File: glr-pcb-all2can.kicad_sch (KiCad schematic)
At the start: 19 parts, among them J1 Conn_02x04_Top_Bottom, J2 DA15_Pins_MountingHoles, U1 STM32F303K8T6, U2 173020536, U3 173010535

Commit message: add in- and outputs
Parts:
- added J3: Conn_01x04, Connector_PinSocket_2.54mm:PinSocket_1x04_P2.54mm_Vertical, symbol Connector_Generic:Conn_01x04
- renumbered C3 to C1, C4 to C2, C2 to C3, C6 to C4, C7 to C6, D2 to D1, D3 to D2, D4 to D3, D5 to D4, J2 to J1, J1 to J2, R5 to R1, R6 to R2
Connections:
- net +3.3V is gone; now on net +3V3: C1.2, C3.2, J2.5 (Pin_5), R1.1, R3.2, R4.2, U1.1 (VDD), U1.17 (VDD), U1.5 (VDDA)
- net Input filter/5_IN_INT: now reaches U1.10 (PA4)
- net Input filter/6_IN_INT: now reaches U1.11 (PA5)
- net Input filter/7_IN_INT: now reaches U1.12 (PA6)
- net Output/1_OUT_INT: now reaches U1.14 (PB0)
- net Output/2_OUT_INT: now reaches U1.15 (PB1)
- net at U1.25 (PA15): now also J3.4 (Pin_4)
- net at U1.26 (PB3): now also J3.1 (Pin_1)
- net at U1.27 (PB4): now also J3.2 (Pin_2)
- net at U1.28 (PB5): now also J3.3 (Pin_3)
- net Output/3_OUT_INT: now reaches U1.29 (PB6)
- net Output/4_OUT_INT: now reaches U1.30 (PB7)
- net Input filter/1_IN_INT: now reaches U1.6 (PA0)
- net Input filter/2_IN_INT: now reaches U1.7 (PA1)
- net Input filter/3_IN_INT: now reaches U1.8 (PA2)
- net Input filter/4_IN_INT: now reaches U1.9 (PA3)
- net Input filter/6_IN: now reaches J1.10 (P10)
- net Input filter/7_IN: now reaches J1.11 (P111)
- net 1_OUT: now reaches J1.12 (P12)
- net 2_OUT: now reaches J1.13 (P13)
- net 3_OUT: now reaches J1.14 (P14)
- net 4_OUT: now reaches J1.15 (P15)
- net Input filter/1_IN: now reaches J1.5
- net Input filter/2_IN: now reaches J1.6
- net Input filter/3_IN: now reaches J1.7
- net Input filter/4_IN: now reaches J1.8
- net Input filter/5_IN: now reaches J1.9 (P9)
- no-connect marks 1 -> 5
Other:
- sheet CAN Transciever renamed CAN transciever
- added sheet Input filter (input-filter.kicad_sch)
- added sheet Output (output.kicad_sch)
- note added: "24V to 3V3V"
- note added: "24V to 5V"
- note added: "Optional SPI"
- moved on the sheet: C3, C5, C6, D1, D2, J2, R3, R4

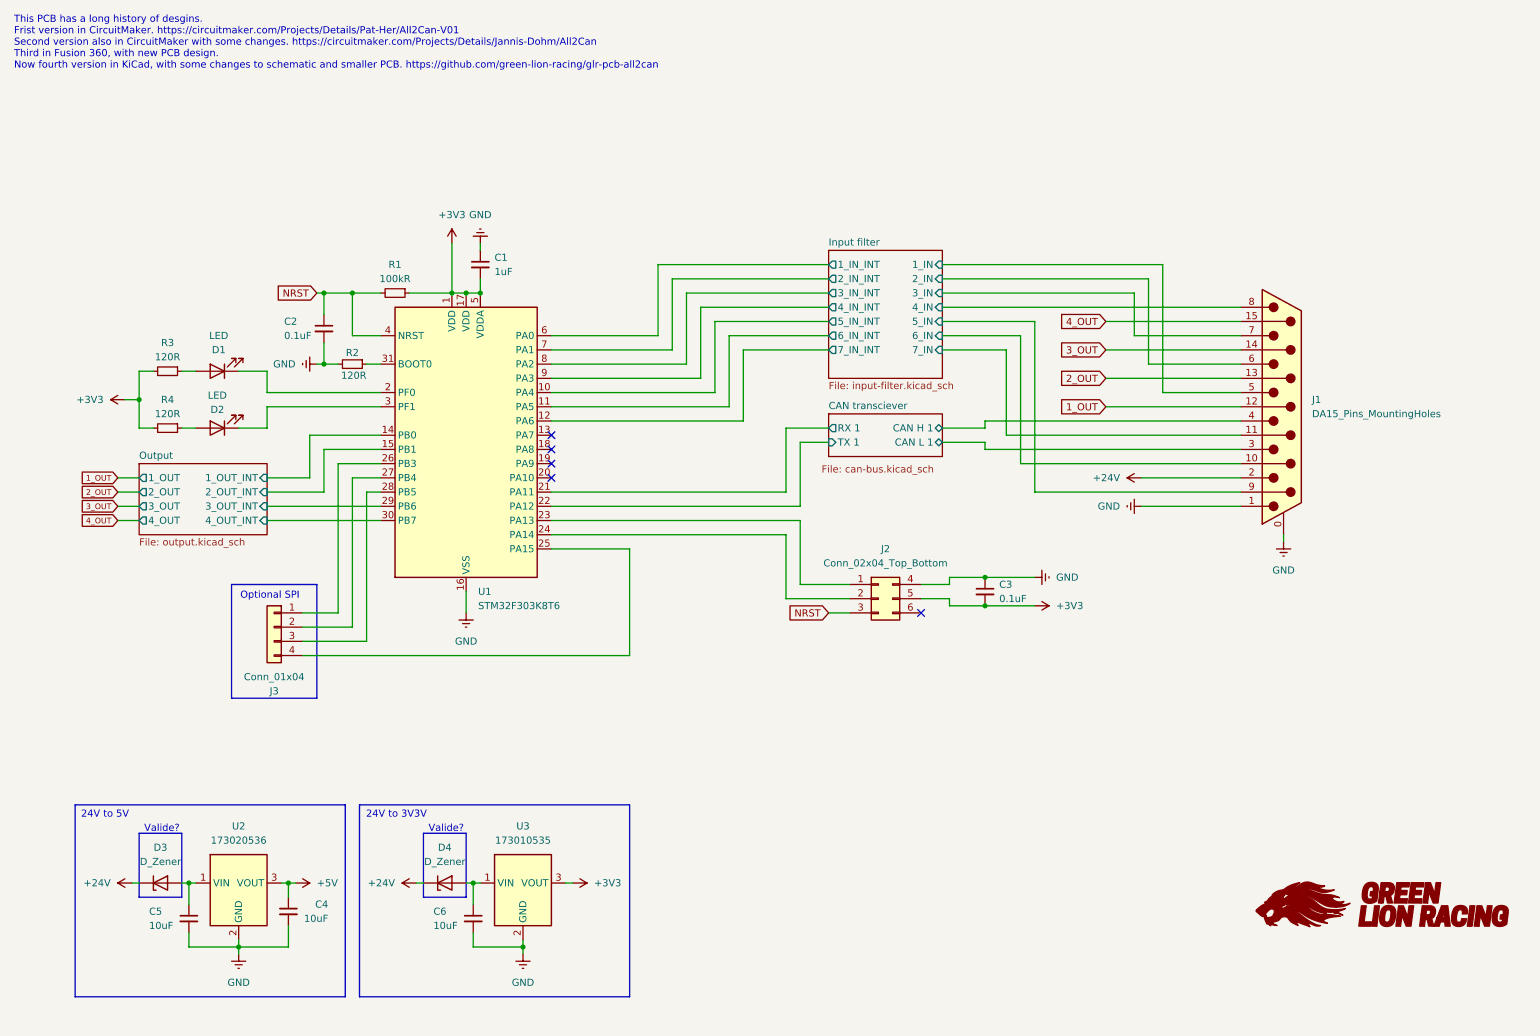
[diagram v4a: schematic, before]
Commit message: change voltage regulators
change can transciever
add more useful parts to can setup
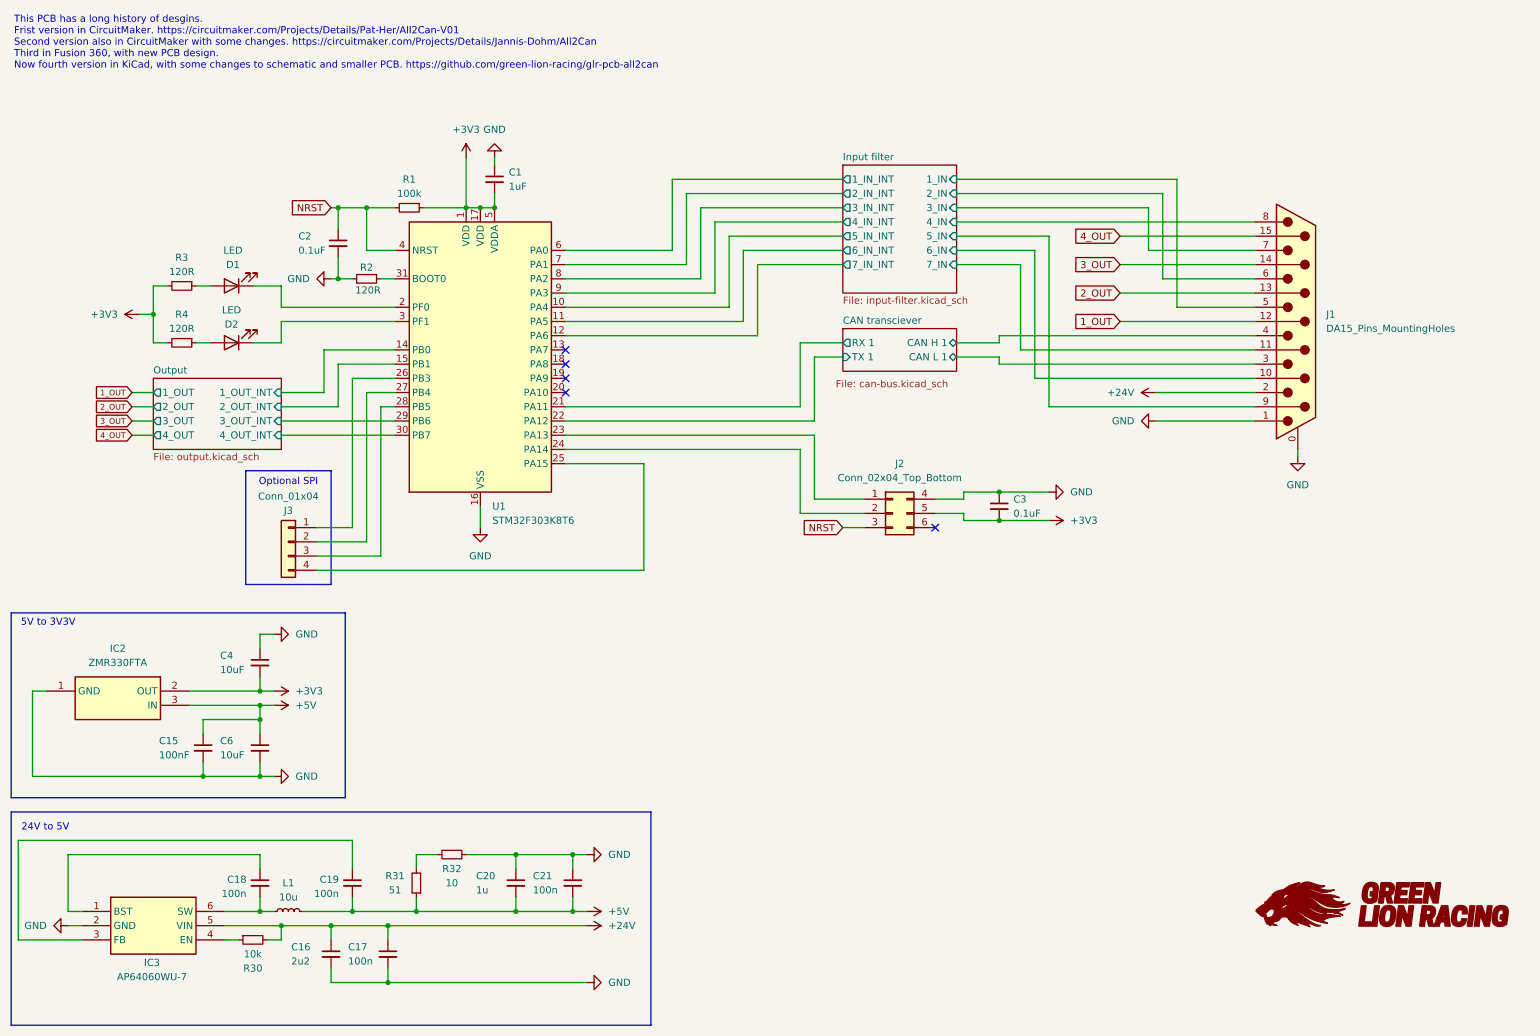
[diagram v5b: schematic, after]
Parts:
- removed C5: 10uF, symbol Device:C_Small
- removed D3, D4: D_Zener, symbol Device:D_Zener
- removed U2: 173020536, MagIC_THT_Wurth:U_Wurth_MagIC-FDSM_17302xx36, symbol Würth MagIC FDSM:173020536
- removed U3: 173010535, MagIC_THT_Wurth:U_Wurth_MagIC-FDSM_17301xx35, symbol Würth MagIC FDSM:173010535
- added C15: 100nF, symbol Device:C_Small
- added C16: 2u2, symbol Device:C_Small
- added C17, C18, C19, C21: 100n, symbol Device:C_Small
- added C20: 1u, symbol Device:C_Small
- added IC2: ZMR330FTA, ZMR330FTA, symbol SamacSys_Parts:ZMR330FTA
- added IC3: AP64060WU-7, SOT95P280X100-6N, symbol SamacSys_Parts:AP64060WU-7
- added L1: 10u, symbol Device:L_Small
- added R30: 10k, symbol Device:R_Small
- added R31: 51, symbol Device:R_Small
- added R32: 10, symbol Device:R_Small
- R1: value 100kR -> 100k
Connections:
- net +24V: now also C16.1, C17.1, IC3.5 (VIN), R30.2
- net +3V3: now also C4.2, IC2.2 (OUT)
- net +5V: now also C6.1, C15.1, C19.2, C20.2, C21.2, IC2.3 (IN), L1.2, R31.1; no longer C4.1
- net GND: now also C4.1, C15.2, C16.2, C17.2, C20.1, C21.1, IC2.1 (GND), IC3.2 (GND), R32.2; no longer C4.2
- new net: R31.2, R32.1
- new net: IC3.4 (EN), R30.1
- new net: C18.1, IC3.1 (BST)
- new net: C18.2, IC3.6 (SW), L1.1
- new net: C19.1, IC3.3 (FB)
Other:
- note added: "5V to 3V3V"
- note removed: "24V to 3V3V"
- note removed: "Valide?"
- moved on the sheet: C1, C2, C3, C6, D1, D2, J1, J2, J3, R1, R2, R3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

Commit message: switch to ic STM32C092KCT6
use more labels
add optional i2c and uart
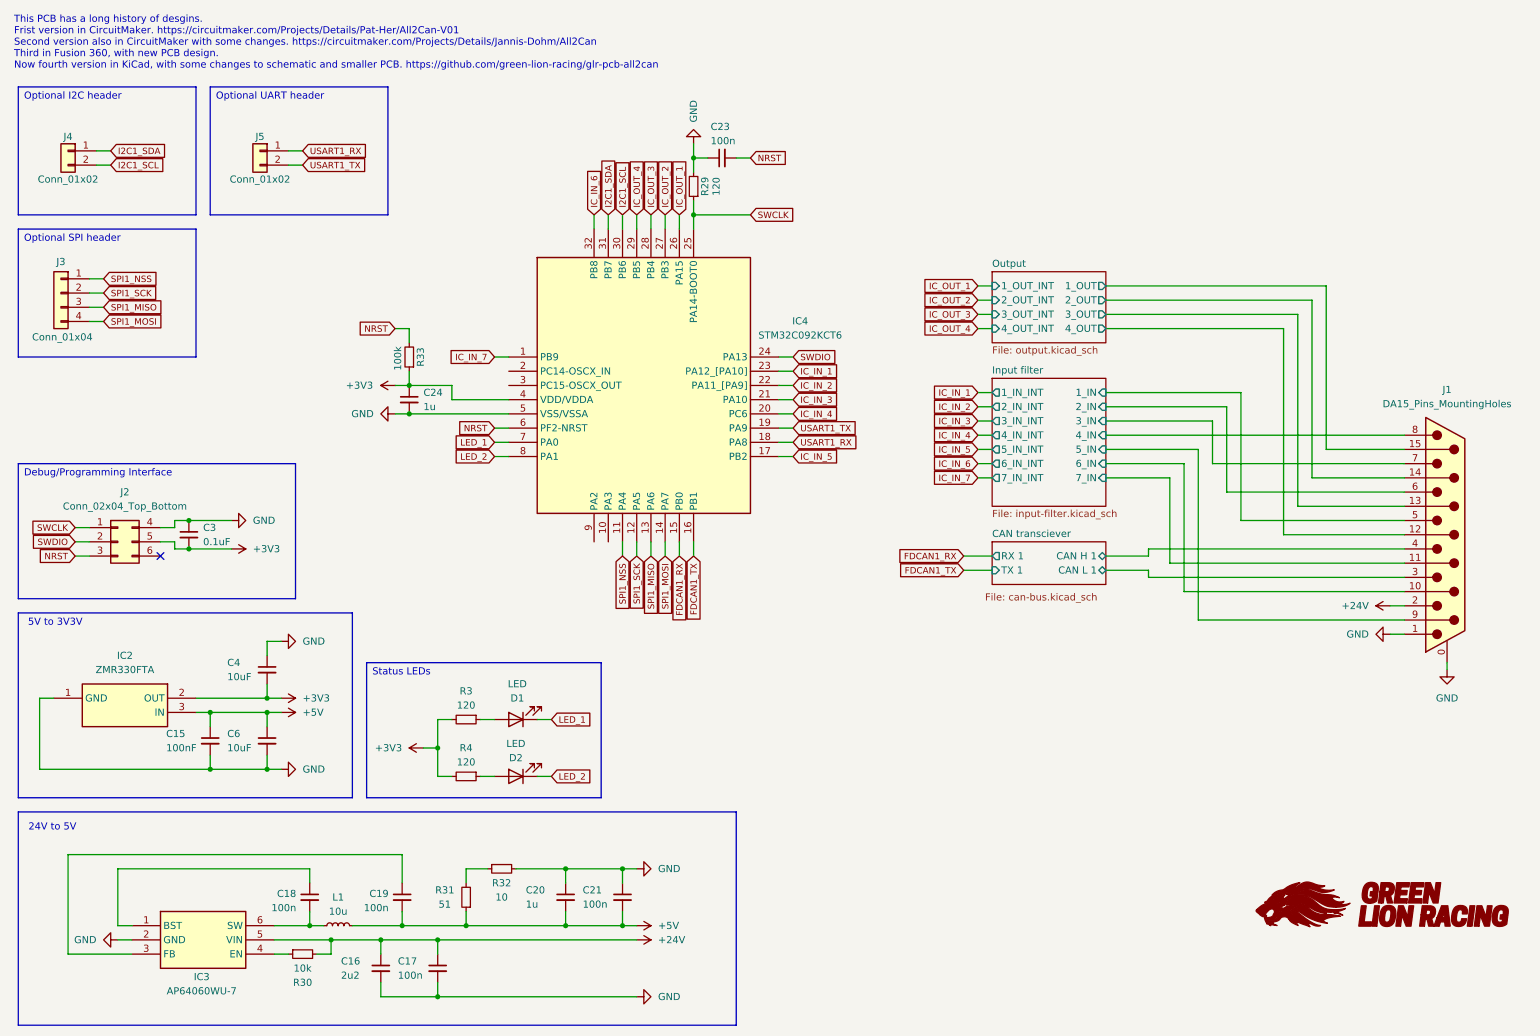
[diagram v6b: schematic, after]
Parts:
- removed C1: 1uF, symbol Device:C_Small
- removed C2: 0.1uF, symbol Device:C_Small
- removed R1: 100k, symbol Device:R_Small
- removed R2: 120R, symbol Device:R_Small
- removed U1: STM32F303K8T6, Package_QFP:LQFP-32_7x7mm_P0.8mm, symbol MCU_ST_STM32F3:STM32F303K8Tx
- added C23: 100n, symbol Device:C_Small
- added C24: 1u, symbol Device:C_Small
- added IC4: STM32C092KCT6, QFP80P900X900X160-32N, symbol SamacSys_Parts:STM32C092KCT6
- added J4, J5: Conn_01x02, Connector_PinSocket_2.54mm:PinSocket_1x04_P2.54mm_Vertical, symbol Connector_Generic:Conn_01x02
- added R29: 120, symbol Device:R_Small
- added R33: 100k, symbol Device:R_Small
- R3, R4: value 120R -> 120
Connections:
- net +3V3: now also C24.1, IC4.4 (VDD/VDDA), R33.1
- net GND: now also C23.1, C24.2, IC4.5 (VSS/VSSA), R29.2
- net NRST: now also C23.2, IC4.6 (PF2-NRST), R33.2
- net LED_1: now reaches D1.1 (K)
- net LED_1: now also IC4.7 (PA0)
- net SWCLK: now reaches J2.1 (Pin_1)
- net SWCLK: now also IC4.25 (PA14-BOOT0), R29.1
- net SWDIO: now reaches J2.2 (Pin_2)
- net SWDIO: now also IC4.24 (PA13)
- net SPI1_MOSI: now reaches J3.4 (Pin_4)
- net SPI1_MOSI: now also IC4.14 (PA7)
- net SPI1_NSS: now reaches J3.1 (Pin_1)
- net SPI1_NSS: now also IC4.11 (PA4)
- net SPI1_SCK: now reaches J3.2 (Pin_2)
- net SPI1_SCK: now also IC4.12 (PA5)
- net SPI1_MISO: now reaches J3.3 (Pin_3)
- net SPI1_MISO: now also IC4.13 (PA6)
- net LED_2: now reaches D2.1 (K)
- net LED_2: now also IC4.8 (PA1)
- net 1_OUT renamed Output/4_OUT
- net 2_OUT renamed Output/3_OUT
- net 3_OUT renamed Output/2_OUT
- net 4_OUT renamed Output/1_OUT
- new net FDCAN1_RX: IC4.15 (PB0)
- new net FDCAN1_TX: IC4.16 (PB1)
- new net I2C1_SCL: IC4.30 (PB6), J4.2 (Pin_2)
- new net I2C1_SDA: IC4.31 (PB7), J4.1 (Pin_1)
- new net IC_IN_1: IC4.23 (PA12_[PA10])
- new net IC_IN_2: IC4.22 (PA11_[PA9])
- new net IC_IN_3: IC4.21 (PA10)
- new net IC_IN_4: IC4.20 (PC6)
- new net IC_IN_5: IC4.17 (PB2)
- new net IC_IN_6: IC4.32 (PB8)
- new net IC_IN_7: IC4.1 (PB9)
- new net IC_OUT_1: IC4.26 (PA15)
- new net IC_OUT_2: IC4.27 (PB3)
- new net IC_OUT_3: IC4.28 (PB4)
- new net IC_OUT_4: IC4.29 (PB5)
- new net USART1_RX: IC4.18 (PA8), J5.1 (Pin_1)
- new net USART1_TX: IC4.19 (PA9), J5.2 (Pin_2)
- no-connect marks 5 -> 1
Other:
- note added: "Debug/Programming Interface"
- note added: "Optional I2C header"
- note added: "Optional SPI header"
- note added: "Optional UART header"
- note added: "Status LEDs"
- note removed: "Optional SPI"
- moved on the sheet: C15, C16, C17, C18, C19, C20, C21, C3, C4, C6, D1, D2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

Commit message: added 6 axis imu LSM6DSV16BXTR
fixed link in in input filter
removed optional i2c
add not connected elements to ic
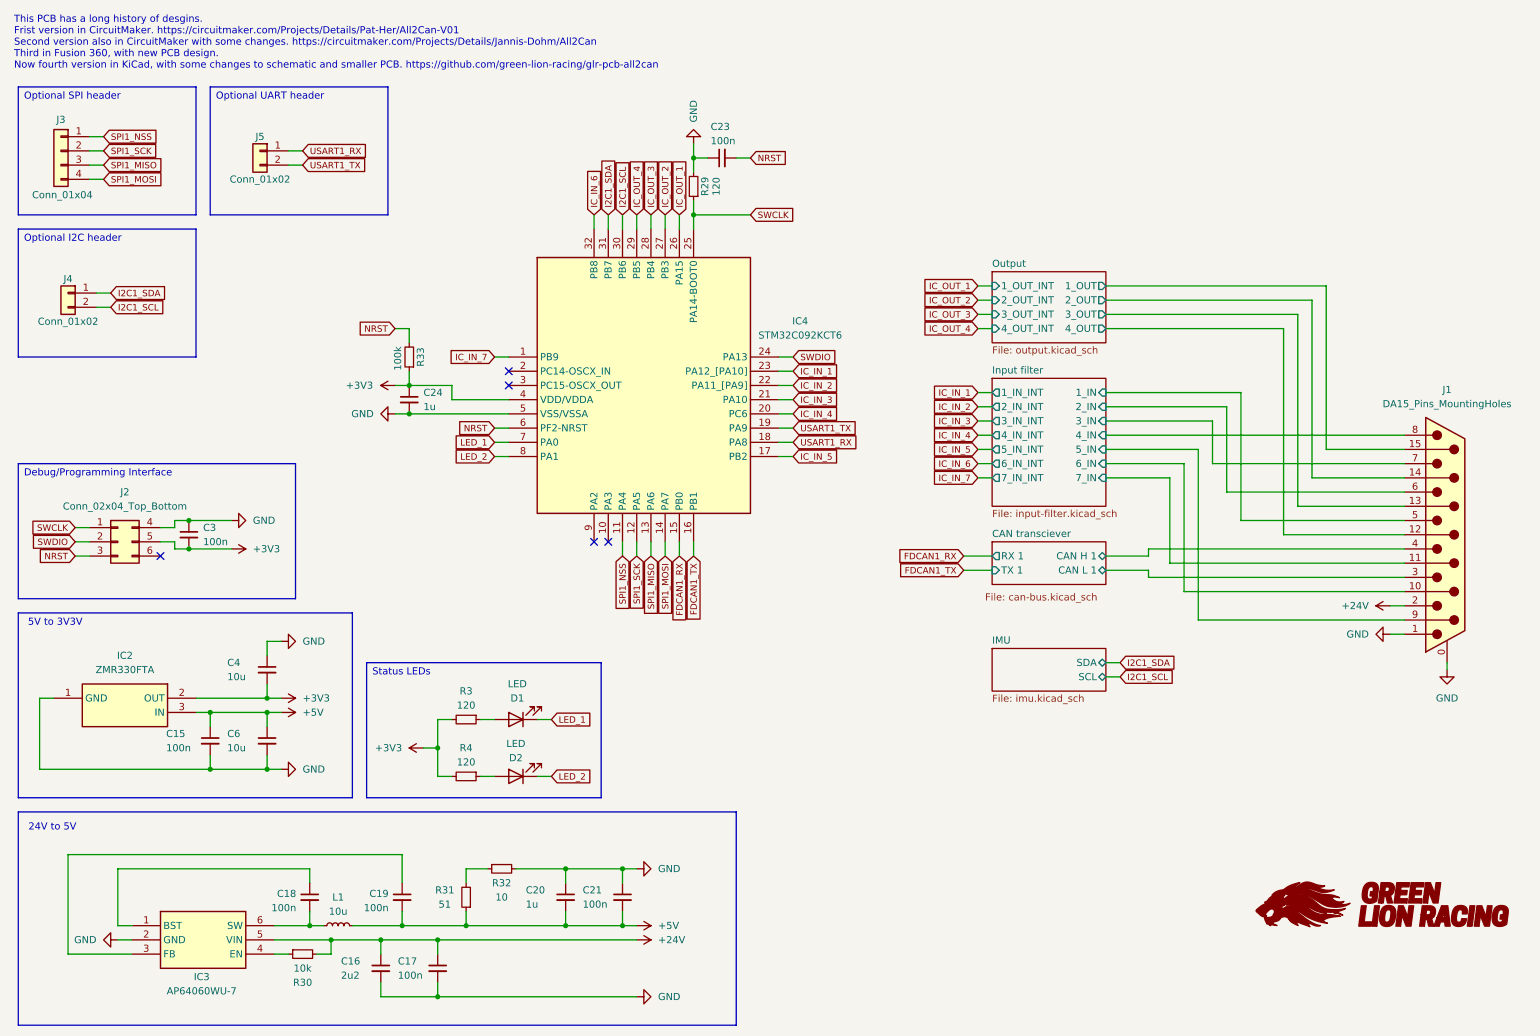
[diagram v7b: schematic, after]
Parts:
- C15: value 100nF -> 100n
- C3: value 0.1uF -> 100n
- C4, C6: value 10uF -> 10u
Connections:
- no-connect marks 1 -> 5
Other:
- added sheet IMU (imu.kicad_sch)
- moved on the sheet: J3
